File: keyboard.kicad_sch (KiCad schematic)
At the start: 0 parts

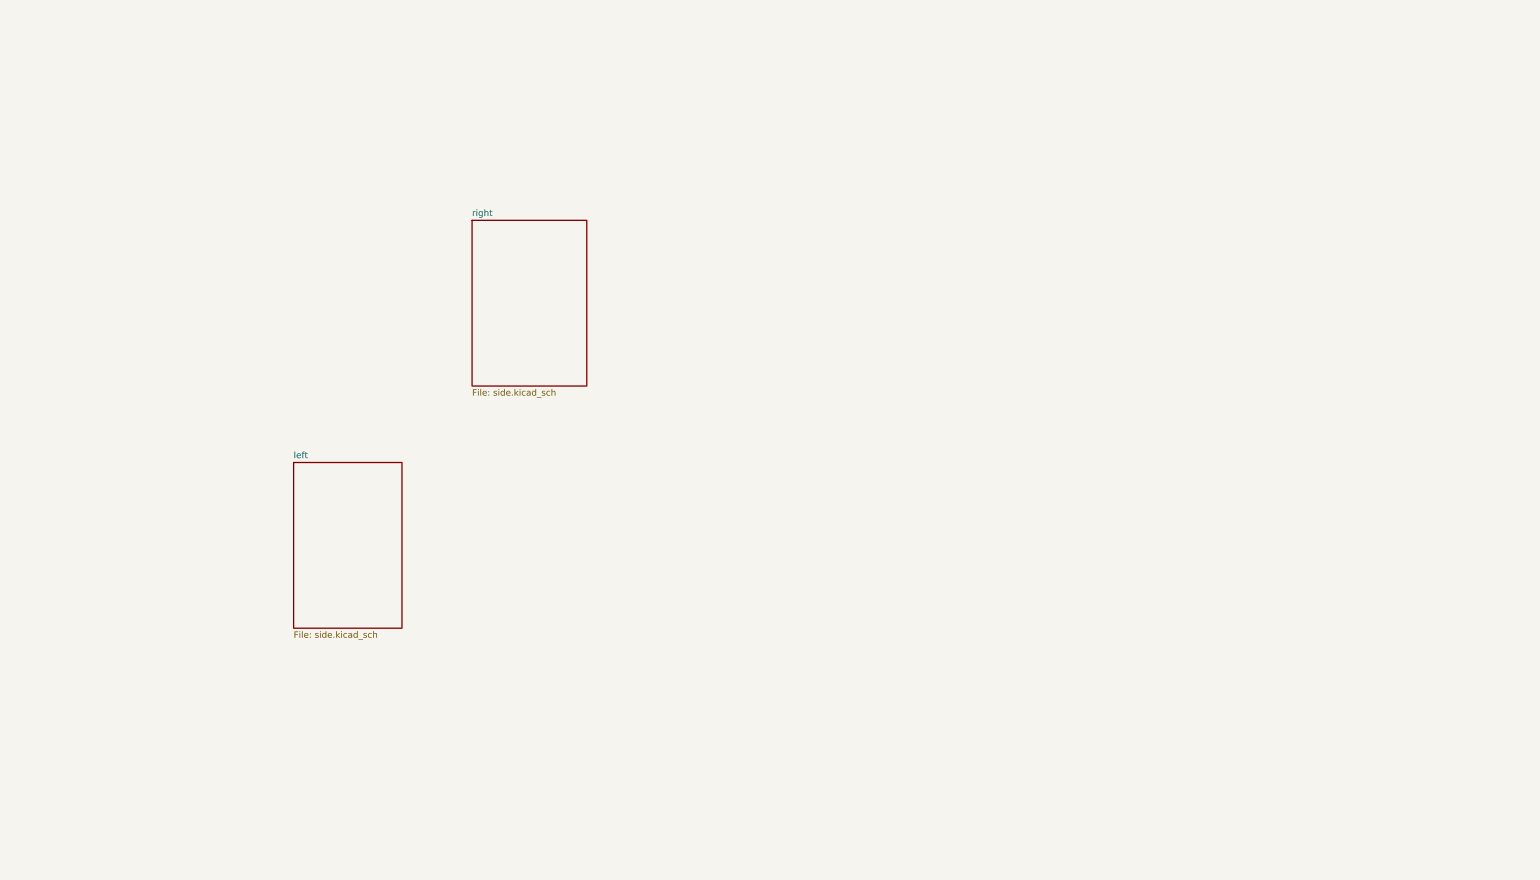
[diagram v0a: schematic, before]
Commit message: Changed keyboard layout to 4*13
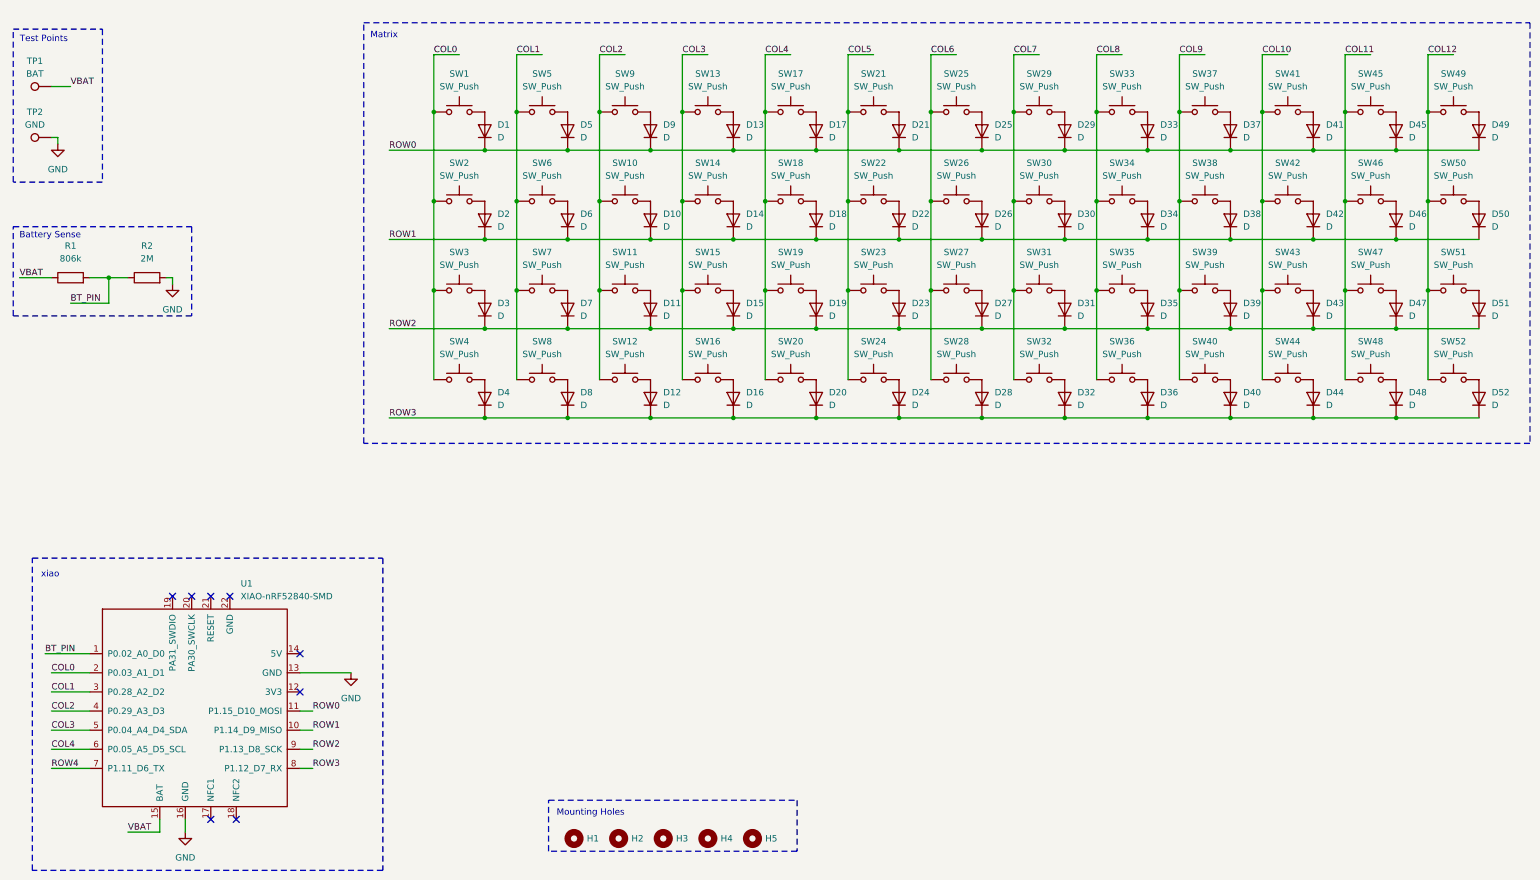
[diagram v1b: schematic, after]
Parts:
- added D1, D10, D11, D12, D13, D14, D15, D16, D17, D18, D19, D2, D20, D21, D22, D23, D24, D25, D26, D27, D28, D29, D3, D30, D31, D32, D33, D34, D35, D36, D37, D38, D39, D4, D40, D41, D42, D43, D44, D45, D46, D47, D48, D49, D5, D50, D51, D52, D6, D7, D8, D9: D, Diode_SMD:D_SOD-123, symbol Device:D
- added H1, H2, H3, H4, H5: MountingHole, Panelization:mouse-bite-5mm-slot, symbol Mechanical:MountingHole
- added R1: 806k, Resistor_SMD:R_0805_2012Metric, symbol Device:R
- added R2: 2M, Resistor_SMD:R_0805_2012Metric, symbol Device:R
- added SW1, SW10, SW11, SW12, SW13, SW14, SW15, SW16, SW17, SW18, SW19, SW2, SW20, SW21, SW22, SW23, SW24, SW25, SW26, SW27, SW28, SW29, SW3, SW30, SW31, SW32, SW33, SW34, SW35, SW36, SW37, SW38, SW39, SW4, SW40, SW41, SW42, SW43, SW44, SW45, SW46, SW47, SW48, SW49, SW5, SW50, SW51, SW52, SW6, SW7, SW8, SW9: SW_Push, PCM_marbastlib-choc:SW_choc_v1_HS_CPG135001S30_1u, symbol Switch:SW_Push
- added TP1: BAT, TestPoint:TestPoint_Pad_D2.0mm, symbol Connector:TestPoint
- added TP2: GND, TestPoint:TestPoint_Pad_D2.0mm, symbol Connector:TestPoint
- added U1: XIAO-nRF52840-SMD, XIAO:modified-XIAO-nRF52840-SMD, symbol Seeed_Studio_XIAO_Series:XIAO-nRF52840-SMD
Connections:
- new net: D4.2 (A), SW4.2
- new net: D45.2 (A), SW45.2
- new net: D1.2 (A), SW1.2
- new net: D2.2 (A), SW2.2
- new net: D11.2 (A), SW11.2
- new net: D8.2 (A), SW8.2
- new net: D34.2 (A), SW34.2
- new net: D23.2 (A), SW23.2
- new net: D24.2 (A), SW24.2
- new net: D14.2 (A), SW14.2
- new net: D36.2 (A), SW36.2
- new net: D26.2 (A), SW26.2
- new net: D46.2 (A), SW46.2
- new net: D16.2 (A), SW16.2
- new net: D30.2 (A), SW30.2
- new net: D19.2 (A), SW19.2
- new net: D15.2 (A), SW15.2
- new net: D44.2 (A), SW44.2
- new net: D27.2 (A), SW27.2
- new net: D40.2 (A), SW40.2
- new net: D35.2 (A), SW35.2
- new net: D29.2 (A), SW29.2
- new net: D32.2 (A), SW32.2
- new net: D39.2 (A), SW39.2
- new net: D25.2 (A), SW25.2
- new net: D21.2 (A), SW21.2
- new net: D3.2 (A), SW3.2
- new net: D48.2 (A), SW48.2
- new net: D50.2 (A), SW50.2
- new net: D12.2 (A), SW12.2
- new net: D18.2 (A), SW18.2
- new net: D5.2 (A), SW5.2
- new net: D38.2 (A), SW38.2
- new net: D51.2 (A), SW51.2
- new net: D52.2 (A), SW52.2
- new net: D28.2 (A), SW28.2
- new net: D6.2 (A), SW6.2
- new net: D7.2 (A), SW7.2
- new net: D10.2 (A), SW10.2
- new net: D20.2 (A), SW20.2
- new net: D31.2 (A), SW31.2
- new net: D33.2 (A), SW33.2
- new net: D22.2 (A), SW22.2
- new net: D41.2 (A), SW41.2
- new net: D13.2 (A), SW13.2
- new net: D43.2 (A), SW43.2
- new net: D47.2 (A), SW47.2
- new net: D9.2 (A), SW9.2
- new net: D42.2 (A), SW42.2
- new net: D49.2 (A), SW49.2
- new net: D17.2 (A), SW17.2
- new net: D37.2 (A), SW37.2
- new net BT_PIN: R1.2, R2.1, U1.1 (P0.02_A0_D0)
- new net COL0: SW1.1, SW2.1, SW3.1, SW4.1, U1.2 (P0.03_A1_D1)
- new net COL1: SW5.1, SW6.1, SW7.1, SW8.1, U1.3 (P0.28_A2_D2)
- new net COL10: SW41.1, SW42.1, SW43.1, SW44.1
- new net COL11: SW45.1, SW46.1, SW47.1, SW48.1
- new net COL12: SW49.1, SW50.1, SW51.1, SW52.1
- new net COL2: SW10.1, SW11.1, SW12.1, SW9.1, U1.4 (P0.29_A3_D3)
- new net COL3: SW13.1, SW14.1, SW15.1, SW16.1, U1.5 (P0.04_A4_D4_SDA)
- new net COL4: SW17.1, SW18.1, SW19.1, SW20.1, U1.6 (P0.05_A5_D5_SCL)
- new net COL5: SW21.1, SW22.1, SW23.1, SW24.1
- new net COL6: SW25.1, SW26.1, SW27.1, SW28.1
- new net COL7: SW29.1, SW30.1, SW31.1, SW32.1
- new net COL8: SW33.1, SW34.1, SW35.1, SW36.1
- new net COL9: SW37.1, SW38.1, SW39.1, SW40.1
- new net GND: R2.2, TP2.1, U1.13 (GND), U1.16 (GND)
- new net ROW0: D1.1 (K), D13.1 (K), D17.1 (K), D21.1 (K), D25.1 (K), D29.1 (K), D33.1 (K), D37.1 (K), D41.1 (K), D45.1 (K), D49.1 (K), D5.1 (K), D9.1 (K), U1.11 (P1.15_D10_MOSI)
- new net ROW1: D10.1 (K), D14.1 (K), D18.1 (K), D2.1 (K), D22.1 (K), D26.1 (K), D30.1 (K), D34.1 (K), D38.1 (K), D42.1 (K), D46.1 (K), D50.1 (K), D6.1 (K), U1.10 (P1.14_D9_MISO)
- new net ROW2: D11.1 (K), D15.1 (K), D19.1 (K), D23.1 (K), D27.1 (K), D3.1 (K), D31.1 (K), D35.1 (K), D39.1 (K), D43.1 (K), D47.1 (K), D51.1 (K), D7.1 (K), U1.9 (P1.13_D8_SCK)
- new net ROW3: D12.1 (K), D16.1 (K), D20.1 (K), D24.1 (K), D28.1 (K), D32.1 (K), D36.1 (K), D4.1 (K), D40.1 (K), D44.1 (K), D48.1 (K), D52.1 (K), D8.1 (K), U1.8 (P1.12_D7_RX)
- new net ROW4: U1.7 (P1.11_D6_TX)
- new net VBAT: R1.1, TP1.1, U1.15 (BAT)
- no-connect marks 0 -> 8
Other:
- removed sheet left
- removed sheet right
- note added: "Battery Sense"
- note added: "Matrix"
- note added: "Mounting Holes"
- note added: "Test Points"
- note added: "xiao"
- title: (none) -> KeyboardDI52UE

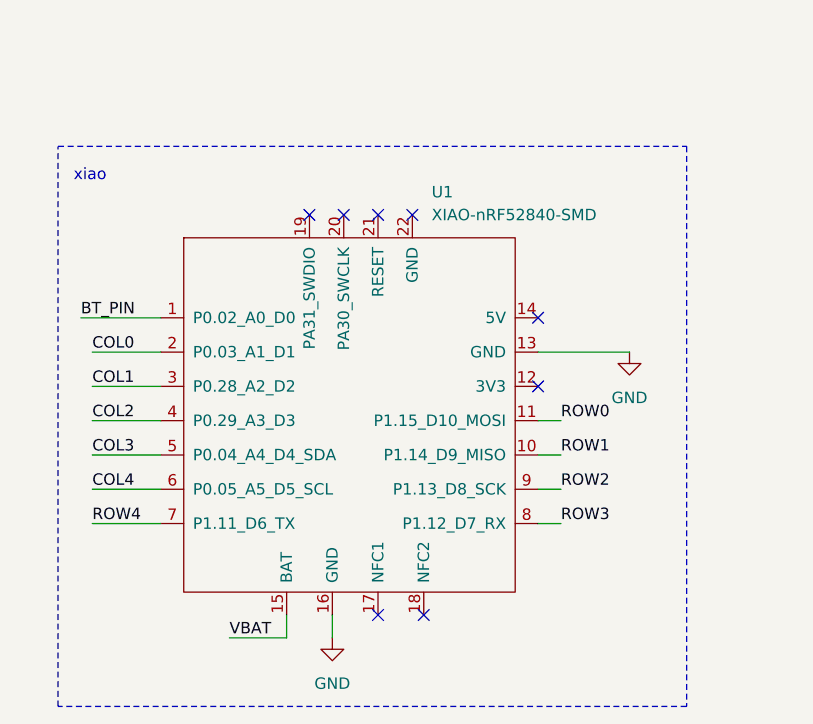
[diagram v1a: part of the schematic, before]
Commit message: Replaced XIAO with ESP32 devoard
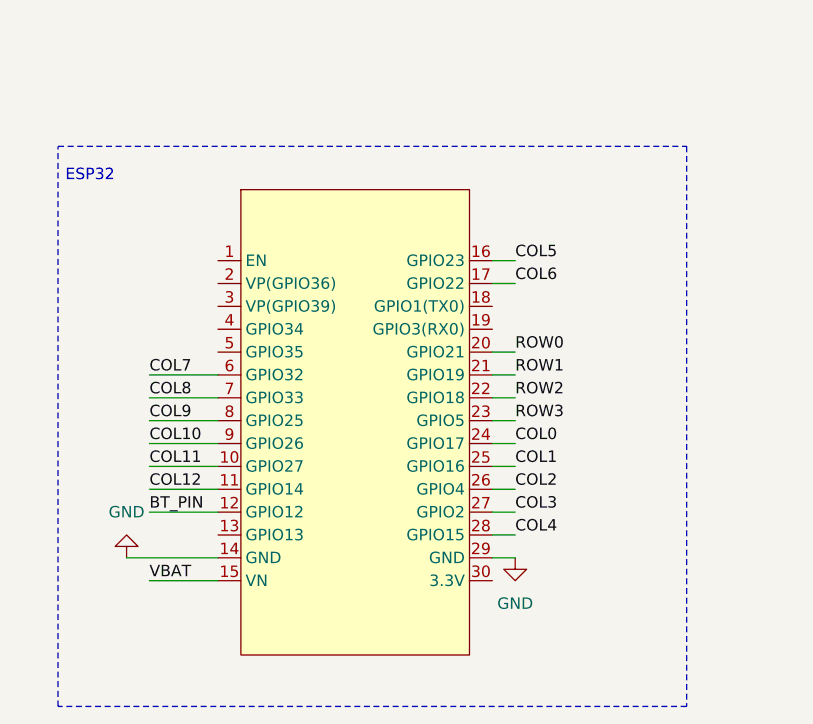
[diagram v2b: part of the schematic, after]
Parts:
- removed U1: XIAO-nRF52840-SMD, XIAO:modified-XIAO-nRF52840-SMD, symbol Seeed_Studio_XIAO_Series:XIAO-nRF52840-SMD
- added U2: ESP32-WROOM-32-DEVBOARD-CH340C, RF_Module:ESP32-WROOM-32D, symbol Custom_ESP32_Library:ESP32-WROOM-32-DEVBOARD-CH340C
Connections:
- net BT_PIN: now also U2.12 (GPIO12)
- net COL0: now also U2.24 (GPIO17)
- net COL1: now also U2.25 (GPIO16)
- net COL10: now also U2.9 (GPIO26)
- net COL11: now also U2.10 (GPIO27)
- net COL12: now also U2.11 (GPIO14)
- net COL2: now also U2.26 (GPIO4)
- net COL3: now also U2.27 (GPIO2)
- net COL4: now also U2.28 (GPIO15)
- net COL7: now also U2.6 (GPIO32)
- net COL8: now also U2.7 (GPIO33)
- net COL9: now also U2.8 (GPIO25)
- net GND: now also U2.14 (GND), U2.29 (GND)
- net ROW0: now also U2.20 (GPIO21)
- net ROW1: now also U2.21 (GPIO19)
- net ROW2: now also U2.22 (GPIO18)
- net ROW3: now also U2.23 (GPIO5)
- net VBAT: now also U2.15 (VN)
- no-connect marks 8 -> 0
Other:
- note added: "ESP32"
- note removed: "xiao"

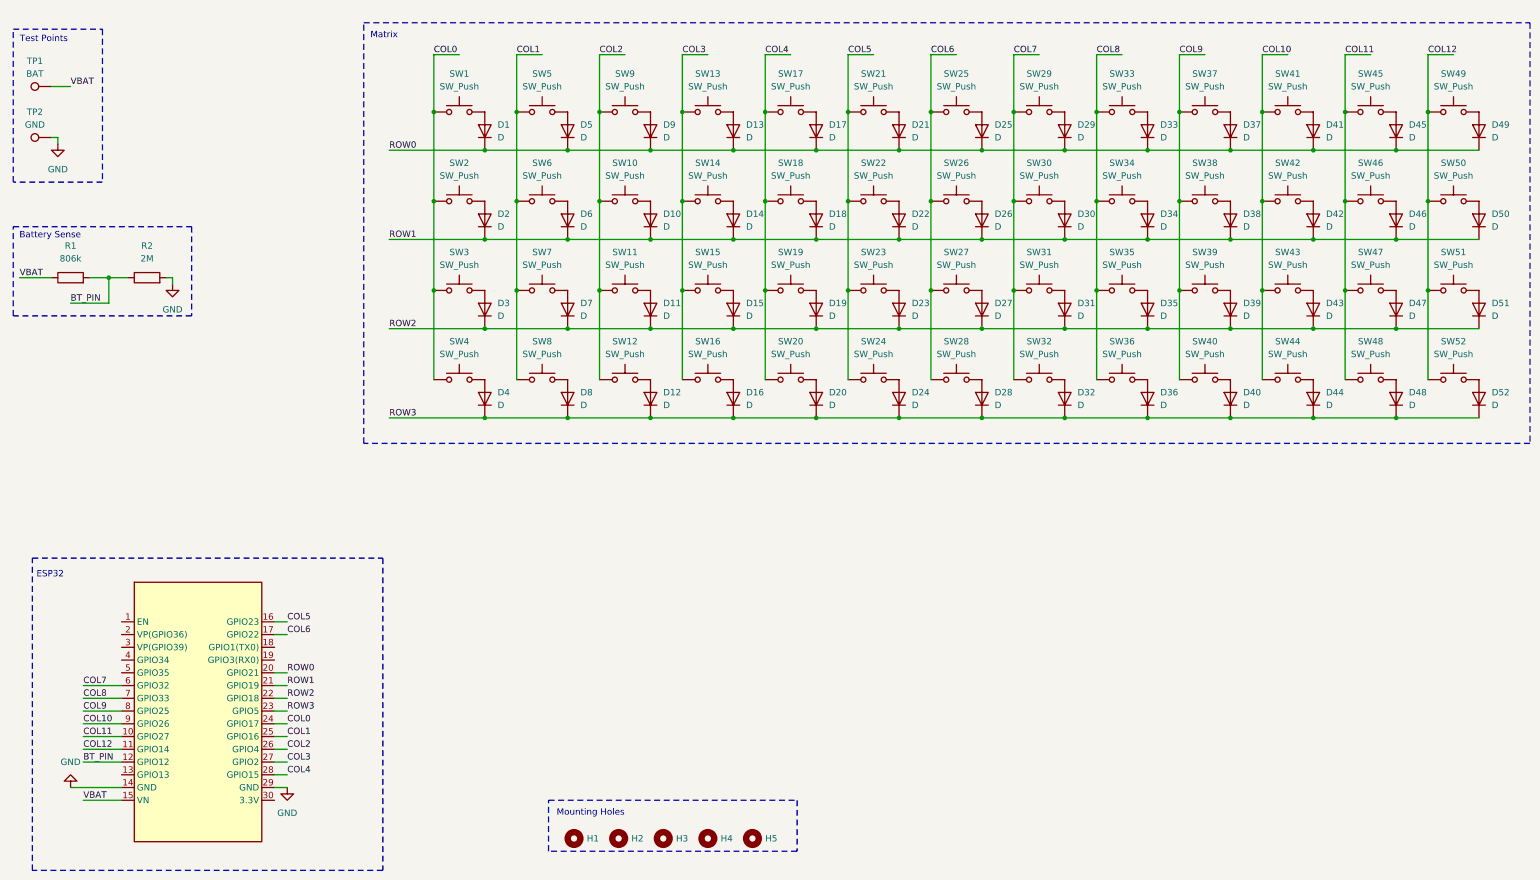
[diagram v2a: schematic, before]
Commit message: Swiched to ESP32 Feather Adafruit HUZZAH32
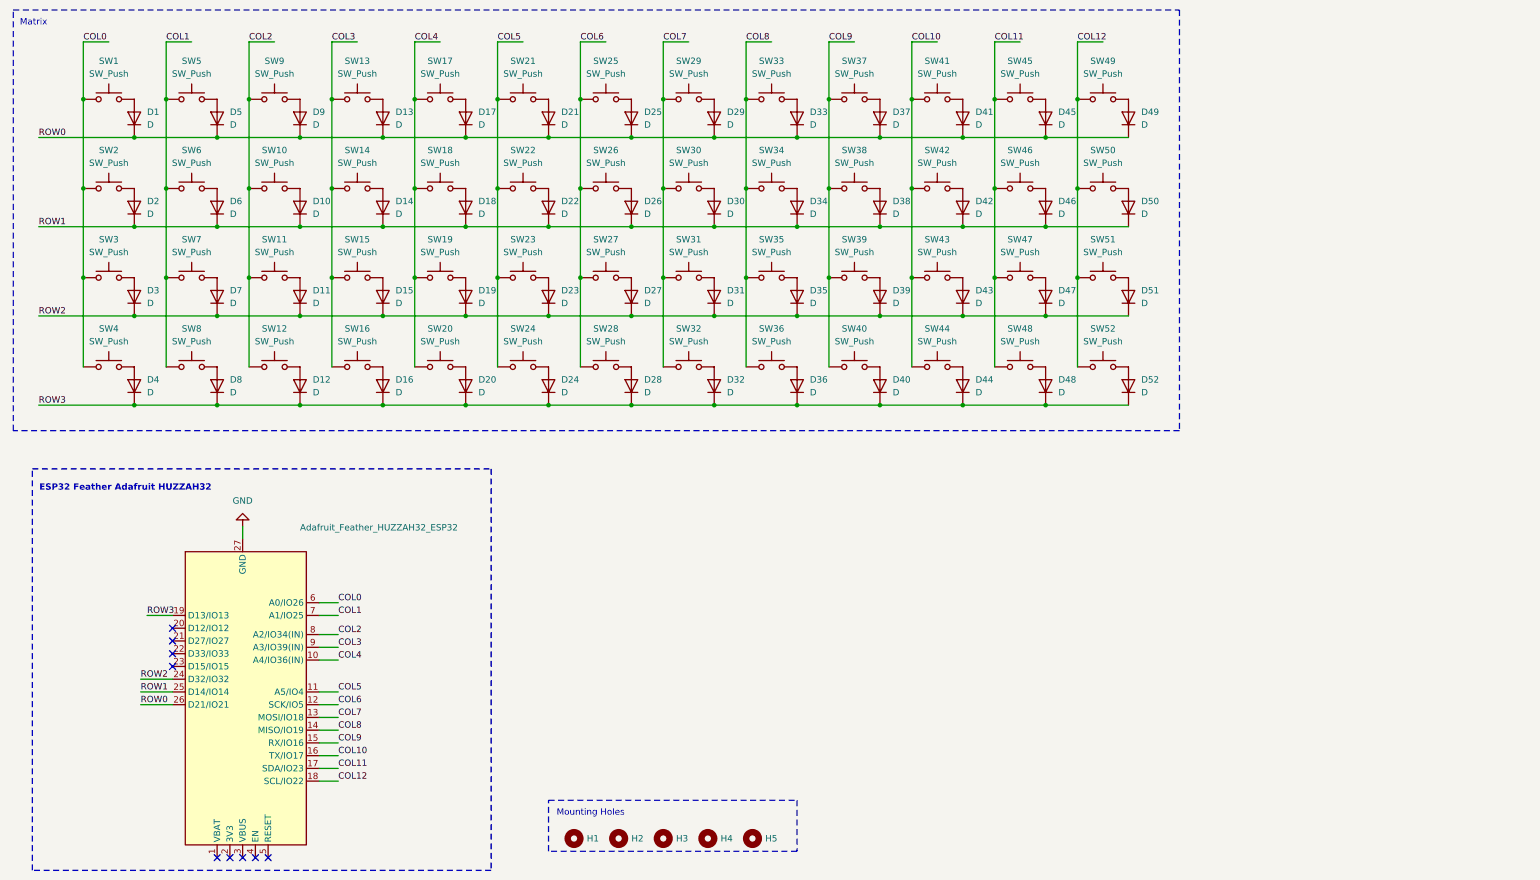
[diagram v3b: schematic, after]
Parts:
- removed R1: 806k, Resistor_SMD:R_0805_2012Metric, symbol Device:R
- removed R2: 2M, Resistor_SMD:R_0805_2012Metric, symbol Device:R
- removed TP1: BAT, TestPoint:TestPoint_Pad_D2.0mm, symbol Connector:TestPoint
- removed TP2: GND, TestPoint:TestPoint_Pad_D2.0mm, symbol Connector:TestPoint
- removed U2: ESP32-WROOM-32-DEVBOARD-CH340C, RF_Module:ESP32-WROOM-32D, symbol Custom_ESP32_Library:ESP32-WROOM-32-DEVBOARD-CH340C
- added A1: Adafruit_Feather_HUZZAH32_ESP32, Module:Adafruit_Feather, symbol Custom_ESP32_Library:Adafruit_Feather_HUZZAH32_ESP32
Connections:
- net COL0: now also A1.6 (A0/IO26)
- net COL1: now also A1.7 (A1/IO25)
- net COL10: now also A1.16 (TX/IO17)
- net COL11: now also A1.17 (SDA/IO23)
- net COL12: now also A1.18 (SCL/IO22)
- net COL2: now also A1.8 (A2/IO34(IN))
- net COL3: now also A1.9 (A3/IO39(IN))
- net COL4: now also A1.10 (A4/IO36(IN))
- net COL5: now also A1.11 (A5/IO4)
- net COL6: now also A1.12 (SCK/IO5)
- net COL7: now also A1.13 (MOSI/IO18)
- net COL8: now also A1.14 (MISO/IO19)
- net COL9: now also A1.15 (RX/IO16)
- net GND: now also A1.27 (GND)
- net ROW0: now also A1.26 (D21/IO21)
- net ROW1: now also A1.25 (D14/IO14)
- net ROW2: now also A1.24 (D32/IO32)
- net ROW3: now also A1.19 (D13/IO13)
- no-connect marks 0 -> 9
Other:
- note added: "ESP32 Feather Adafruit HUZZAH32"
- note removed: "Battery Sense"
- note removed: "ESP32"
- note removed: "Test Points"
- moved on the sheet: D1, D10, D11, D12, D13, D14, D15, D16, D17, D18, D19, D2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
